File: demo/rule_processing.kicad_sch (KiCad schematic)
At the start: 0 parts

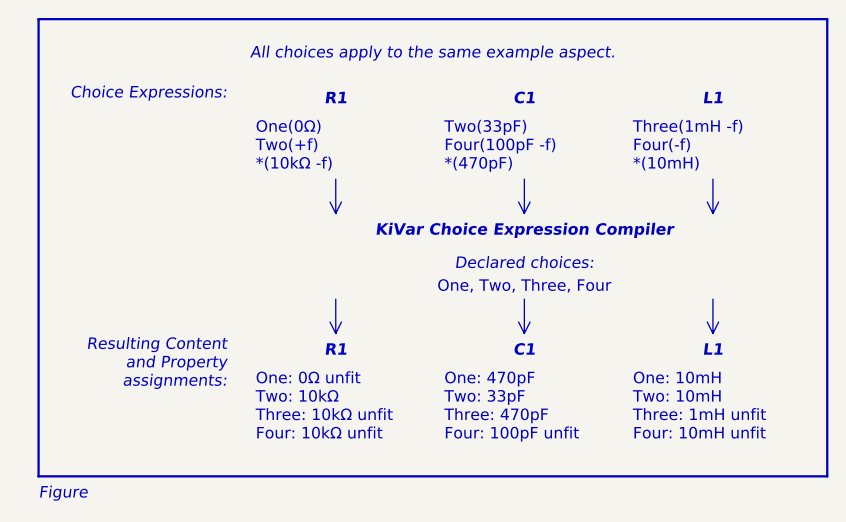
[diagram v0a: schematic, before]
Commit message: Demo project: Use Stand-In choices where useful
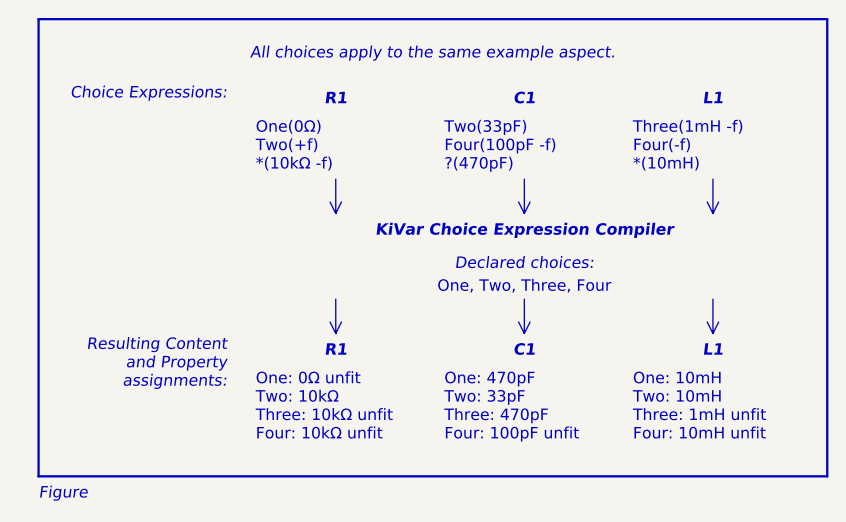
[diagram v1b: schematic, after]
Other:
- note added: "Two(33pF) Four(100pF -f) ?(470pF)"
- note removed: "Two(33pF) Four(100pF -f) *(470pF)"
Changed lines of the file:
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@@
 	(title_block
 		(title "KiVar Demo")
-		(date "2024-07-21")
+		(date "2024-08-17")
 		(rev "0.4.0")
 		(company "Author: Mark Hämmerling <dev@markh.de>")
@@
 		)
 	)
-	(text "Two(33pF)\nFour(100pF -f)\n*(470pF)"
+	(text "Two(33pF)\nFour(100pF -f)\n?(470pF)"
 		(exclude_from_sim no)
 		(at 93.345 44.45 0)
